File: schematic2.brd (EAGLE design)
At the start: 101.6 x 53.3 mm, 77 parts, among them IC6 DS3231/SO

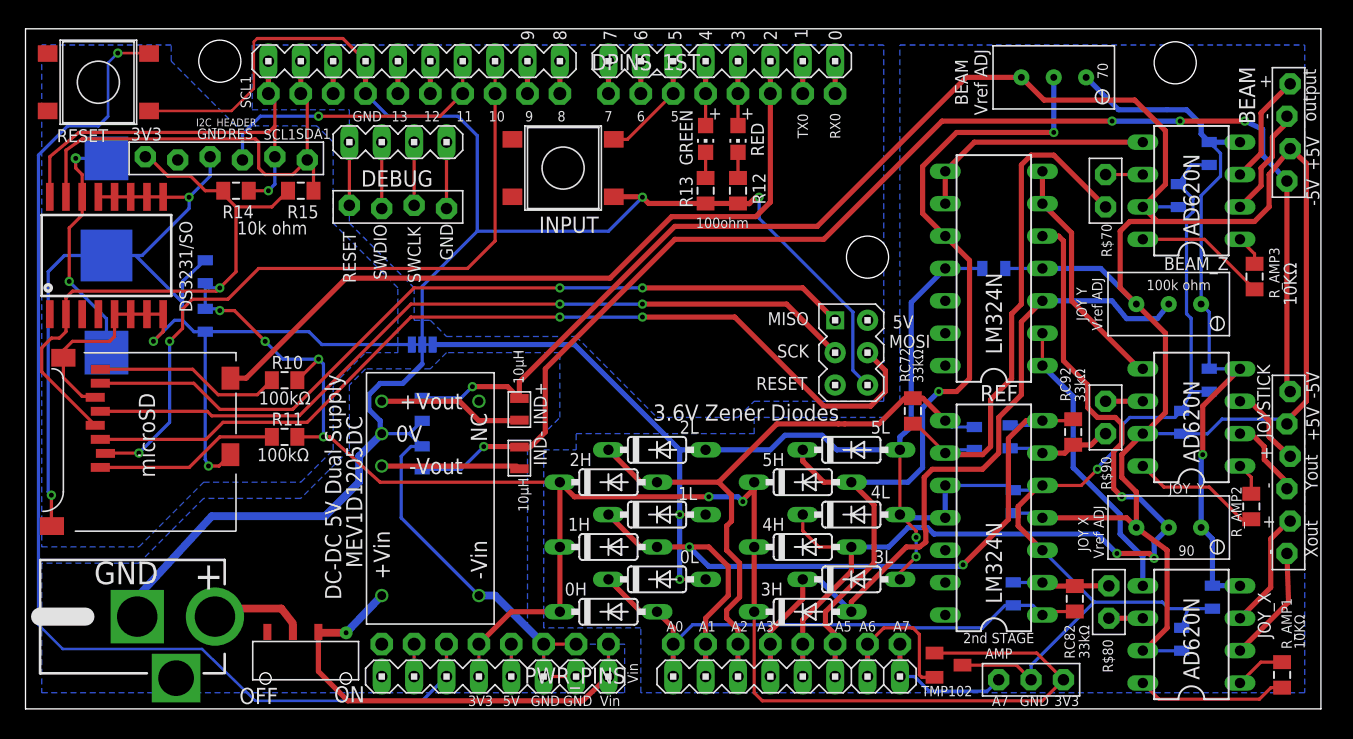
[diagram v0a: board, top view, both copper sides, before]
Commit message: Renamed a bunch of the resistors and capacitors so that they are in a more sensible order on the board.
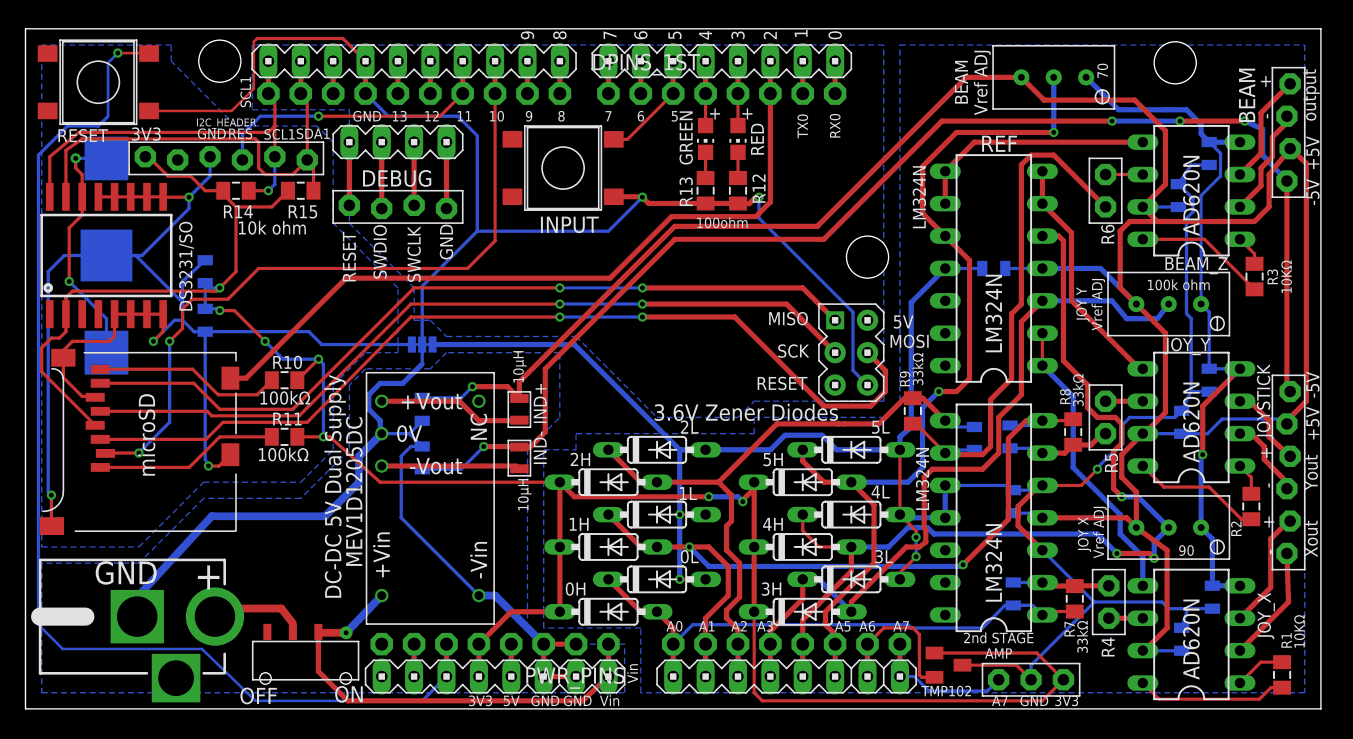
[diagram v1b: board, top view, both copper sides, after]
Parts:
- removed C17, C71: 0.1µF, Felicia_force_logger:0805
- added C10, C9: 0.1µF, Felicia_force_logger:0805
- moved C6 79.8 mm to (92.8, 43.6)
- moved C7 65.9 mm to (77.5, 16.3), turned to 270 degrees
- renumbered C16 to C8, C70 to C5, C72 to C13, C80 to C1, C81 to C2, C82 to C11, C90 to C3, C91 to C4, C92 to C12, R$70 to R6, R$80 to R4, R$90 to R5, RC72 to R9, RC82 to R7, RC92 to R8, R_AMP1 to R1, R_AMP2 to R2, R_AMP3 to R3
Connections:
- net +3V3: now also C10.1, C9.1; no longer C6.1, C7.1
- net +5V: now also C7.2; no longer C17.2
- net AGND: now also C6.2, C7.1; no longer C17.1, C71.2
- net DGND: now also C10.2, C9.2; no longer C6.2, C7.2
- net VNEG: now also C6.1; no longer C71.1
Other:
- board text added: "LM324N"
